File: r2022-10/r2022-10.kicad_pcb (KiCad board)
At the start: 4 copper layers, 100 x 80 mm, 130 parts, among them J1 Conn_01x03_Male, J2 USB_A male UP, J3 USB_B_Micro (up), J4 USB_A (female down), J5 USB_A_Stacked, J6 USB_A_Stacked, J7 USB_A_Stacked, J8 Conn_01x06, Q1 Si4435, U1 2k i2c eeprom, U10 APL3511C, U11 NUP4202, U12 NUP4202, U13 NUP4202, U14 NUP4202, U15 NUP4202, U16 NUP4202, U17 NUP4202, U18 SiC437AED, U19 SE5120ST33, U2 NUP4202, U3 USB2517, U4 APL3511C, U5 APL3511C, U6 APL3511C, U7 APL3511C, U8 APL3511C, U9 APL3511C, Y1 24MHz

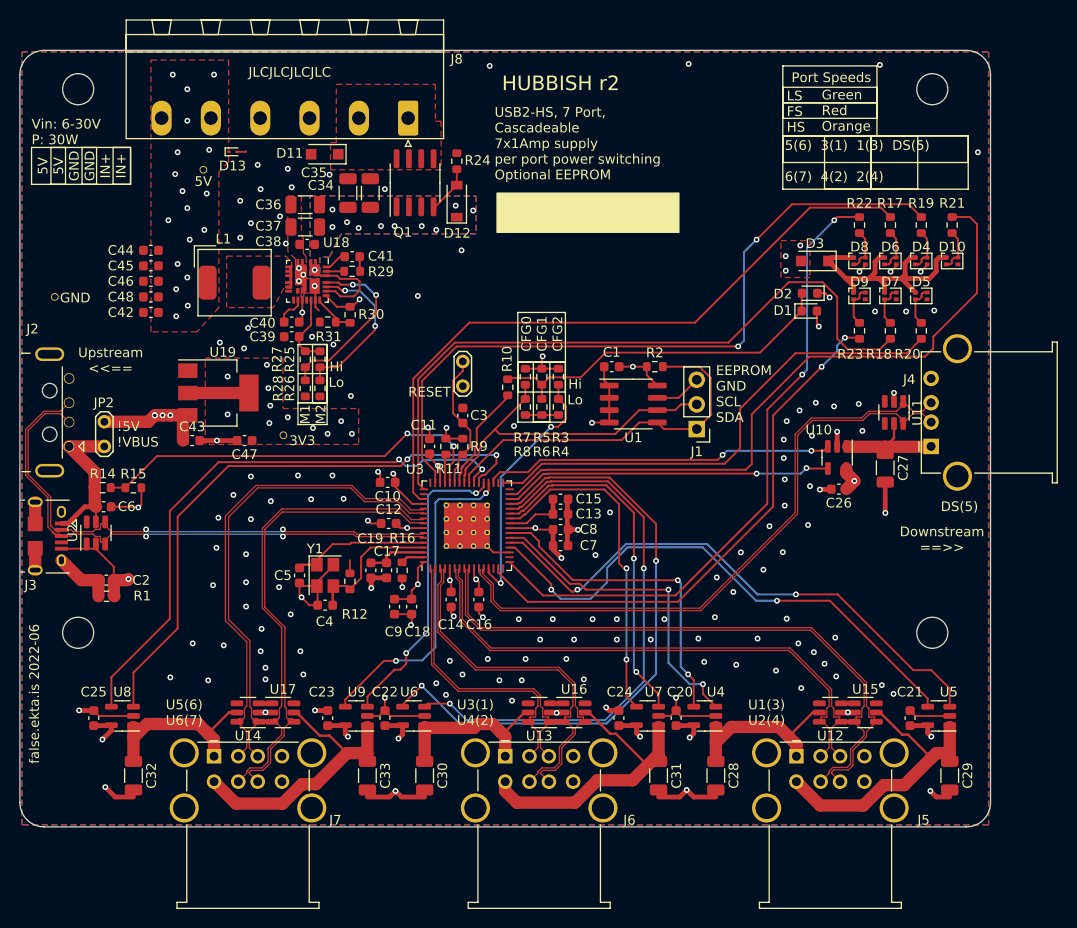
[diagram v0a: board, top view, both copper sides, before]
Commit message: r3: add power good led, add auto switch 5v sources
copied from nanopi usb sections.

still need to adjust the spacing of the leds, and decide on ordering,
with or without eeprom permanently.
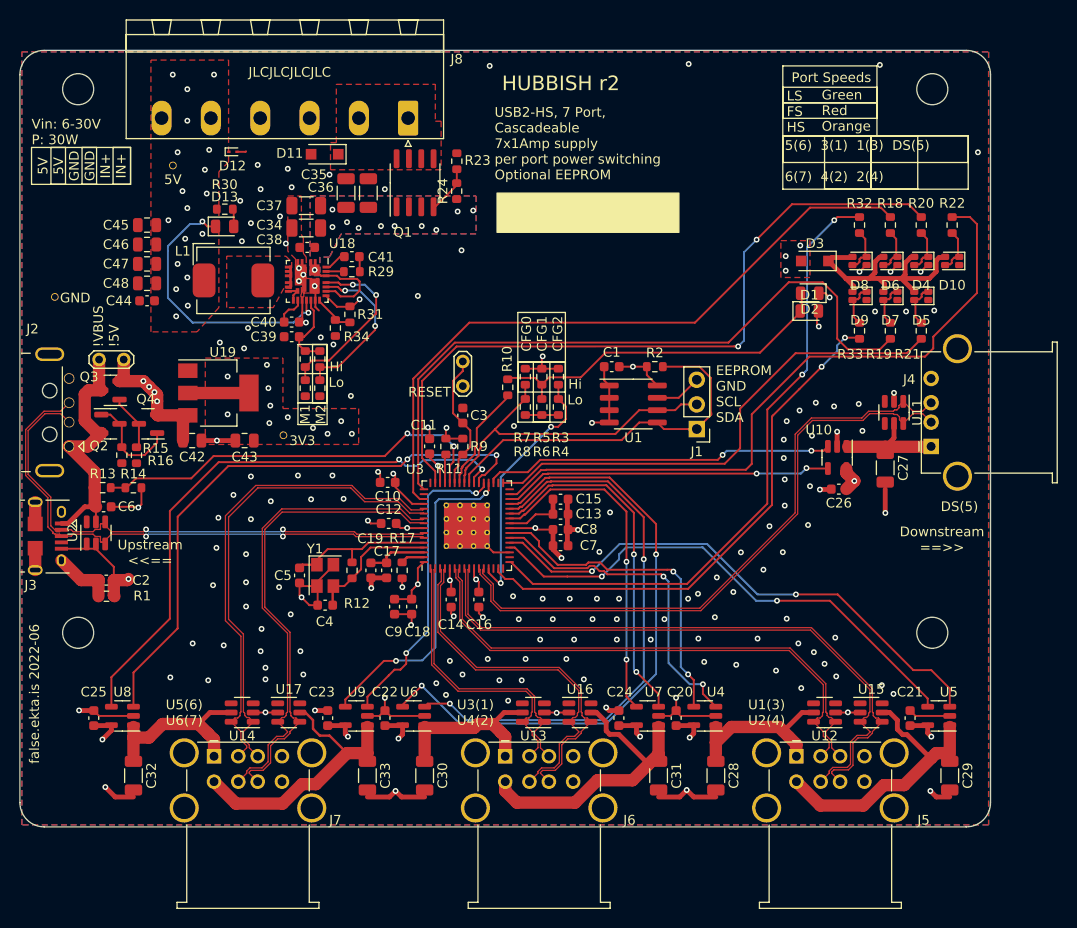
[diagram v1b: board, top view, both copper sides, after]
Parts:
- removed the C42 at (93.5, 97.0)
- removed the D12 at (125.0, 85.5)
- added C47: 10uF, Capacitor_SMD:C_0805_2012Metric, F.Cu at (93.1, 92.0)
- added D13: HS1B, LED_SMD:LED_0805_2012Metric, F.Cu at (101.1, 88.1)
- added Q2: S8550, Package_TO_SOT_SMD:SOT-23, F.Cu at (89.3, 108.5)
- added Q3: AO3401A, Package_TO_SOT_SMD:SOT-23, F.Cu at (89.3, 105.0)
- added Q4: S8550, Package_TO_SOT_SMD:SOT-23, F.Cu at (93.2, 108.5)
- added R15: 10k, Resistor_SMD:R_0603_1608Metric, F.Cu at (90.5, 111.7)
- added R16: 10k, Resistor_SMD:R_0603_1608Metric, F.Cu at (92.0, 111.7)
- added R24: 20k, Resistor_SMD:R_0603_1608Metric, F.Cu at (125.0, 84.5)
- added R34: 10k, Resistor_SMD:R_0603_1608Metric, F.Cu at (112.5, 98.6)
- C42: renamed from C43; footprint Capacitor_SMD:C_0603_1608Metric -> Capacitor_SMD:C_0805_2012Metric
- C43: renamed from C47; footprint Capacitor_SMD:C_0603_1608Metric -> Capacitor_SMD:C_0805_2012Metric
- C44: value 10uF-up? -> 100nF
- C45, C46, C48: value 10uF-up? -> 10uF; footprint Capacitor_SMD:C_0603_1608Metric -> Capacitor_SMD:C_0805_2012Metric
- D1, D2: footprint LED_SMD:LED_0603_1608Metric -> LED_SMD:LED_0805_2012Metric
- D10, D4, D5, D6, D7, D8, D9: value LTST-C295KGKRKT -> LTST-C195KGJRKT; footprint LED_SMD:LED_LiteOn_LTST-C295K -> LED_Dual:T1615_LiteOn_LTST_C195x
- L1: footprint Inductor_SMD:L_AVX_LMLP07A7 -> Inductor_SMD:L_Chilisin_BMRx00060630
- Q1: value Si4435 -> HSM6115
- R30: value 75k -> 330
- R31: value 10k -> 75k
- U19: value SE5120ST33 -> AMS1117-33
- moved R30 16.9 mm to (101.1, 86.4), turned to 180 degrees
- moved JP2 8.97 mm to (88.2, 101.9), turned to 0 degrees
- moved C34 7.52 mm to (109.5, 88.3), turned to 180 degrees
- moved C36 6.61 mm to (115.9, 84.7), turned to 90 degrees
- moved C44 5.22 mm to (93.1, 95.8)
- moved C45 4.22 mm to (93.1, 88.0)
- moved C46 3.81 mm to (93.1, 90.0)
- moved TP1 3.17 mm to (95.8, 81.9)
- moved R31 2.41 mm to (114.0, 97.2), turned to -90 degrees
- moved C37 2.20 mm to (109.5, 86.0)
- moved C48 1.46 mm to (93.1, 94.0)
- moved R12 1.15 mm to (114.2, 123.6)
- moved U17 0.60 mm to (107.7, 138.2)
- moved U12 0.60 mm to (162.9, 138.2)
- moved U13 0.60 mm to (132.9, 138.2)
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- renumbered D13 to D12, R14 to R13, R15 to R14, R16 to R17, R17 to R18, R18 to R19, R19 to R20, R20 to R21, R21 to R22, R24 to R23, R22 to R32, R23 to R33
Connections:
- R30 pad 1: +5V -> Net-(D13-Pad2)
- R30 pad 2: /power_input/fb -> +5V
- R31 pad 1: /power_input/fb -> +5V
- R31 pad 2: GND -> /power_input/fb
- U18 pad 14: unconnected-(U18-Pad14) -> /power_input/pgood
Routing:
- net /power_input/pgood: track 0.00 -> 28.8 mm, vias 0 -> 2
- net +5V: track 59.6 -> 41.6 mm
- net /upstream-config-leds/VBUS_UP: track 17.0 -> 27.4 mm
- net Net-(Q2-Pad1): track 0.00 -> 10.3 mm
- net Net-(Q4-Pad3): track 0.00 -> 5.84 mm
- net /downstream-port-power/EN2: track 56.0 -> 53.1 mm
- net unconnected-(U18-Pad10): track 0.00 -> 2.09 mm
- net Net-(D13-Pad2): track 0.00 -> 1.82 mm
- net /downstream-port-power/OC2: track 57.5 -> 55.8 mm
- net /upstream-config-leds/LED_A7: track 56.1 -> 54.8 mm
- net /downstream-port-power/U2+: track 62.7 -> 63.8 mm
- net /downstream-port-power/U2-: track 62.7 -> 63.7 mm
- net /upstream-config-leds/LED_A6: track 66.7 -> 65.7 mm
- net /downstream-port-power/U6+: track 48.0 -> 48.9 mm
- net /downstream-port-power/U4+: track 36.5 -> 37.5 mm
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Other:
- board text added: "!VBUS !5V"
- board text removed: "!5V !VBUS"

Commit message: r3: reset port leds to be 5mm separation
better for 3mm light pipes.

TODO: shouldn't we move the hub indicicator led into the same block?!
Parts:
- moved R18 8.82 mm to (161.1, 89.9), turned to 0 degrees
- moved D6 8.68 mm to (161.0, 91.7)
- moved D2 8.03 mm to (153.5, 96.6)
- moved D1 7.99 mm to (153.5, 98.4)
- moved D3 5.69 mm to (157.2, 94.9), turned to -90 degrees
- moved D9 5.68 mm to (161.0, 96.7)
- moved R33 5.45 mm to (161.1, 98.5), turned to 180 degrees
- moved D7 3.94 mm to (166.0, 96.7)
- moved R19 3.64 mm to (166.1, 98.5), turned to 180 degrees
- moved R20 2.62 mm to (171.1, 89.9), turned to 0 degrees
- moved D5 2.33 mm to (171.0, 96.7)
- moved R32 1.95 mm to (166.1, 89.9), turned to 0 degrees
- moved R22 1.91 mm to (176.1, 89.9), turned to 0 degrees
- moved D4 1.86 mm to (171.0, 91.7)
- moved R21 1.84 mm to (171.1, 98.5), turned to 180 degrees
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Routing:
- net /upstream-config-leds/LED_DRIVE: track 28.9 -> 41.5 mm
- net /upstream-config-leds/LED_A1: track 70.0 -> 58.6 mm
- net /upstream-config-leds/LED_A2: track 70.2 -> 59.9 mm
- net /upstream-config-leds/CFG_SEL1: track 37.2 -> 29.5 mm, vias 0 -> 2
- net /upstream-config-leds/LED_A3: track 75.9 -> 71.4 mm
- net GND: track 137.2 -> 132.7 mm
- net /upstream-config-leds/LED_A6: track 65.7 -> 62.8 mm
- net /upstream-config-leds/LED_A5: track 70.4 -> 68.7 mm
- net /upstream-config-leds/LA_2-4: track 4.40 -> 3.19 mm
- net /upstream-config-leds/LA_7-6: track 4.40 -> 3.19 mm
- net /upstream-config-leds/LA_4-2: track 4.34 -> 3.19 mm
- net /upstream-config-leds/LA_5-DS: track 4.44 -> 3.42 mm
- net /upstream-config-leds/LA_6-5: track 4.44 -> 3.42 mm
- net /upstream-config-leds/LA_3-1: track 4.44 -> 3.42 mm
- net /upstream-config-leds/LA_1-3: track 4.43 -> 3.42 mm
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
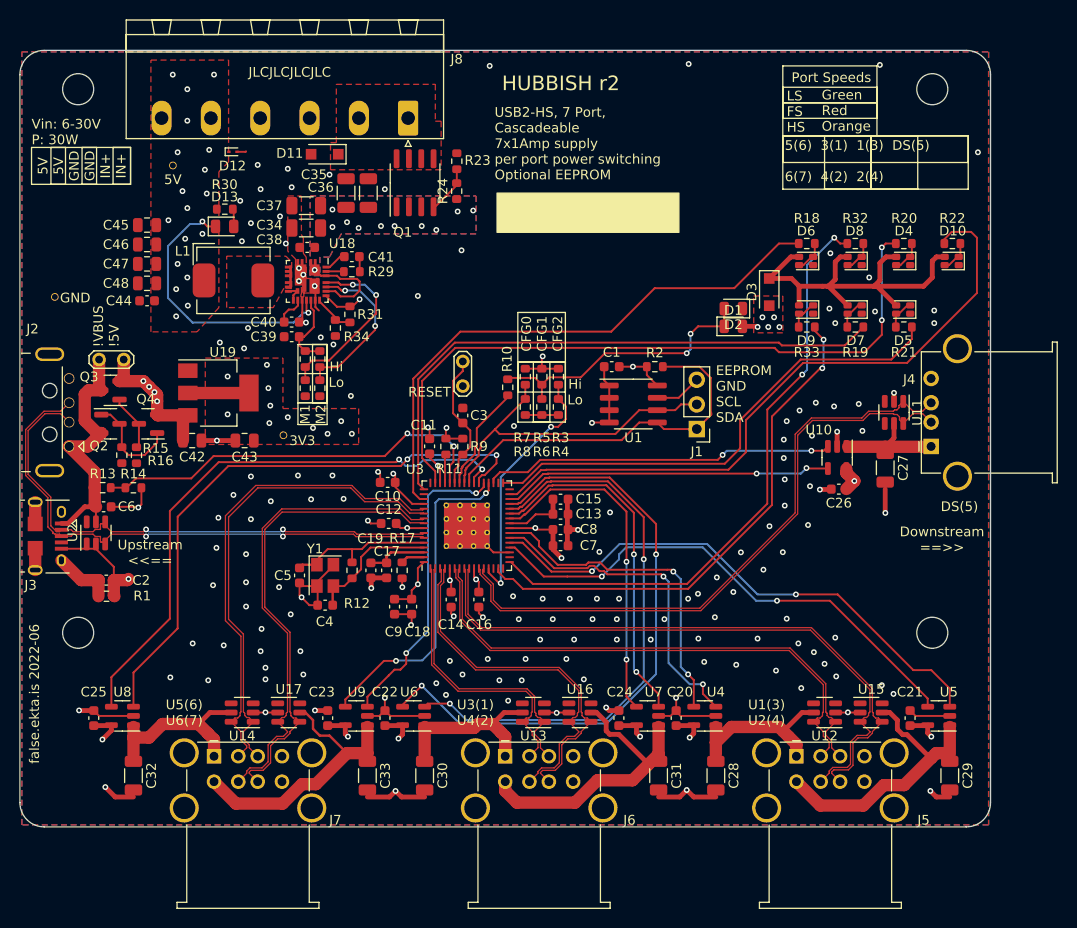
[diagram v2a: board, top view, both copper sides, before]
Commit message: r3: move hub led to same block/spacing
also fixes up a few more traces that got missed when parts were resized
(usb upstream side, and per port downstream power caps)
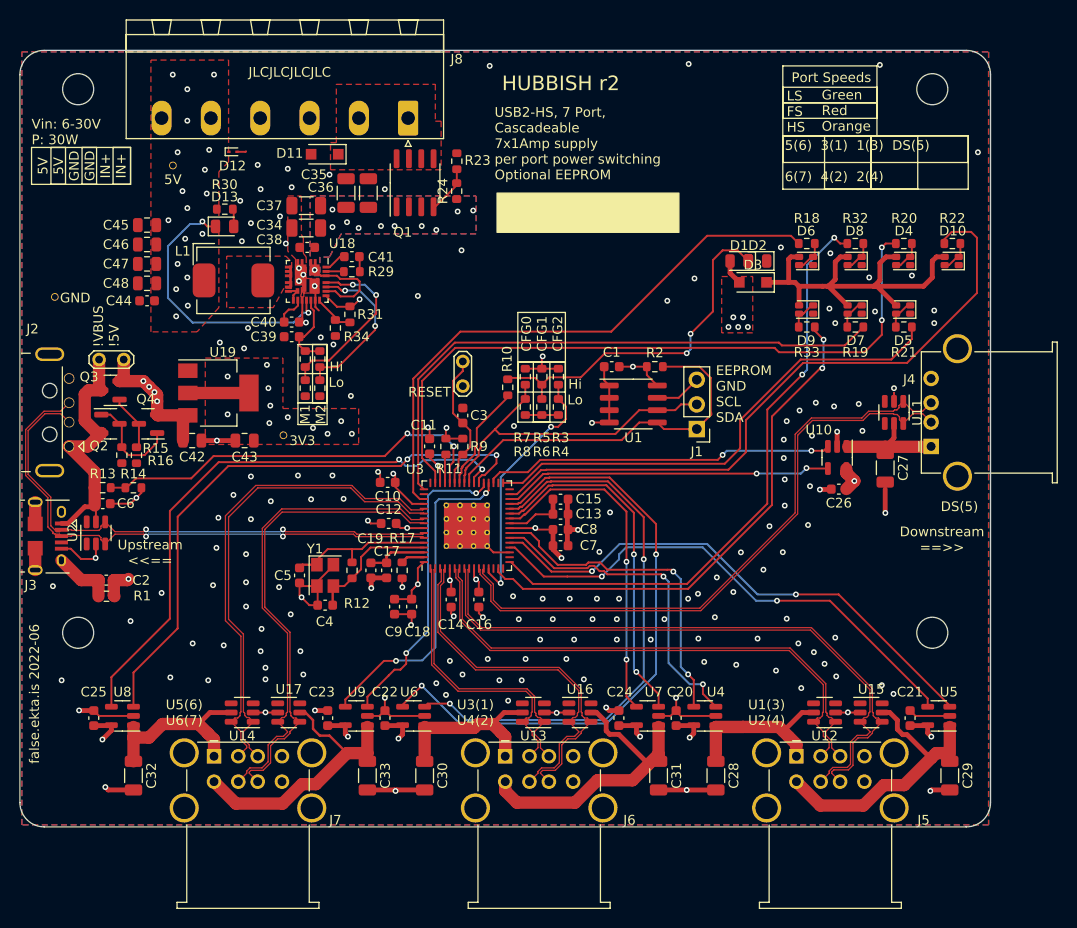
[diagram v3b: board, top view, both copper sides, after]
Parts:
- moved D1 6.76 mm to (154.1, 91.7), turned to 180 degrees
- moved D2 5.50 mm to (156.0, 91.7)
- moved D3 1.96 mm to (155.5, 93.9), turned to 180 degrees
- moved C6 0.33 mm to (88.5, 116.7)
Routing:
- net /upstream-config-leds/CFG_SEL1: track 29.5 -> 36.9 mm
- net GND: track 132.7 -> 127.6 mm, vias 155 -> 164
- net /downstream-port-power/OC2: track 55.8 -> 54.8 mm
- net +3V3: track 51.4 -> 52.4 mm
- net /downstream-port-power/VBUS5: track 17.9 -> 18.7 mm
- net /upstream-config-leds/LED_A1: track 58.6 -> 59.3 mm
- net /downstream-port-power/VBUS1: track 17.7 -> 17.0 mm

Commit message: r3: "last" tweaks
move silk, cleaned some traces, added better ground shield to DS port,
fattened the 5v distrib vias
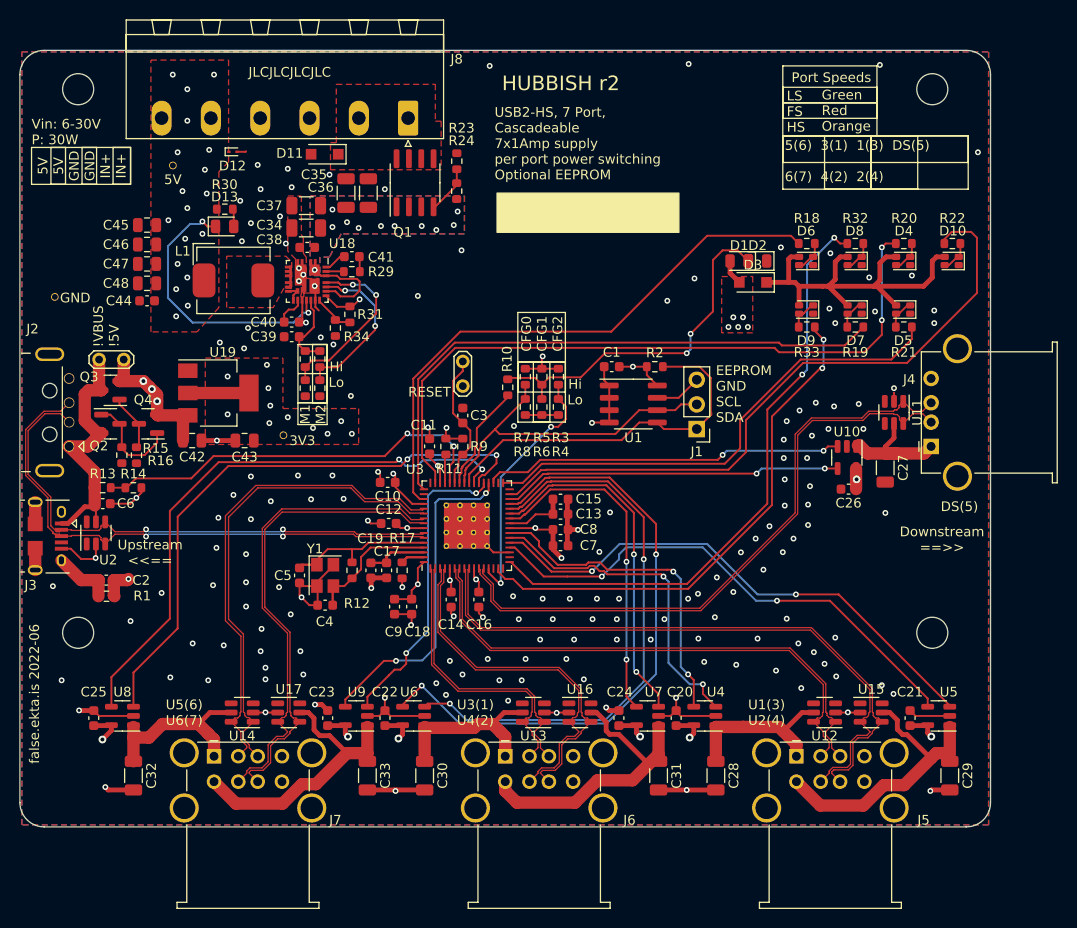
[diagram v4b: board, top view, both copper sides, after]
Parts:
- moved C26 1.00 mm to (165.4, 115.2)
- moved U10 1.00 mm to (165.2, 111.9)
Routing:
- net GND: track 127.6 -> 122.7 mm, vias 164 -> 167
- net /downstream-port-power/VBUS_DS: track 11.3 -> 12.8 mm
- net /downstream-port-power/OC_DS: track 36.3 -> 37.3 mm
- net /downstream-port-power/EN_DS: track 34.1 -> 35.1 mm
- net +5V: track 41.6 -> 41.0 mm, vias 30 -> 29
